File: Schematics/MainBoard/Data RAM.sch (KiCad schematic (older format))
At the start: 8 parts, among them U10 IDT71256SA12TPG, U11 IDT71256SA12TPG, U8 74LS32, U9 74LS04

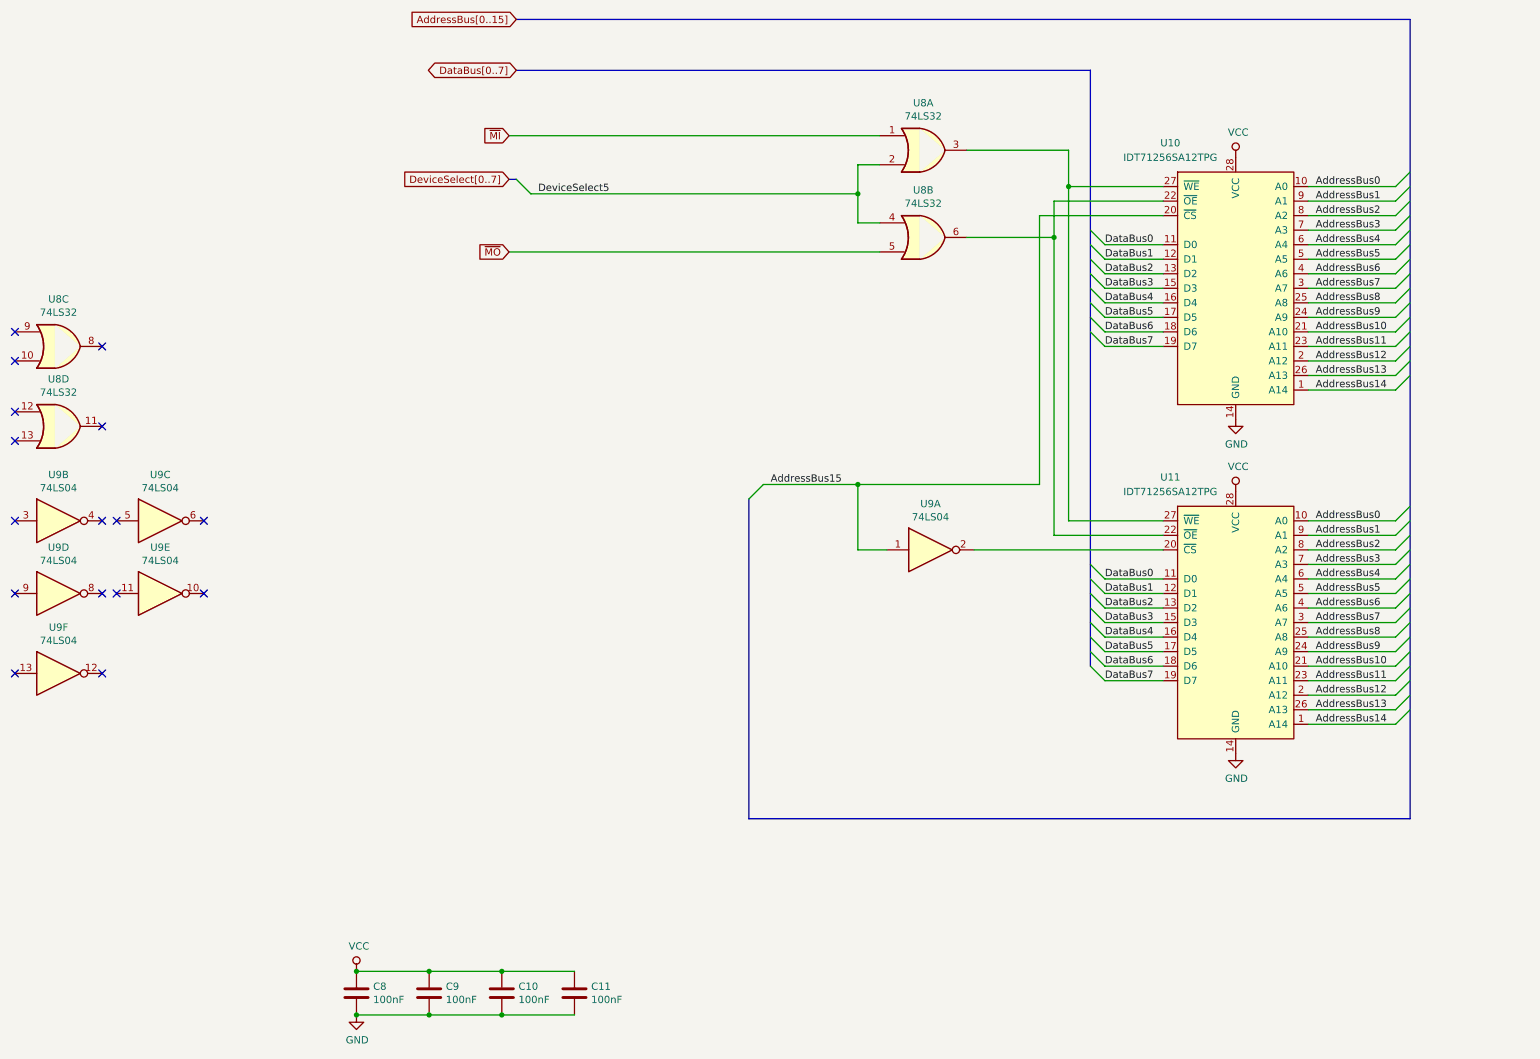
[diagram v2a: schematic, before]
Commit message: Added Data RAM submodule to main board again.
Staked out component positions on the PCB but did not route traces yet.
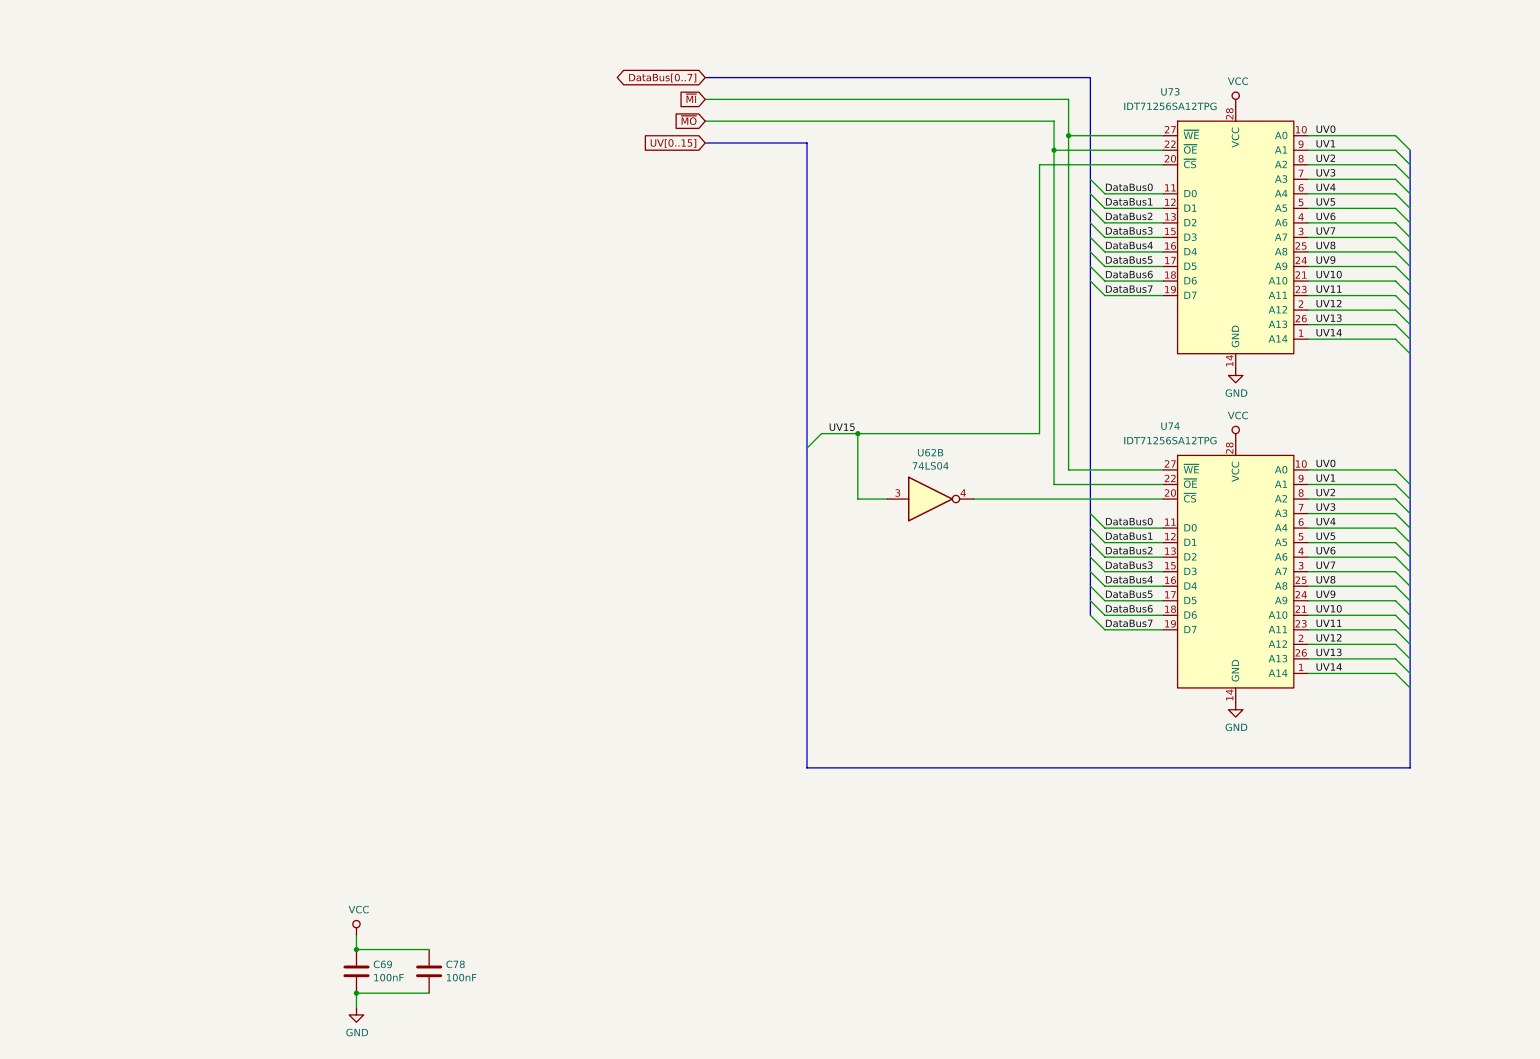
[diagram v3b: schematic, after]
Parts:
- removed C10, C11: 100nF, Capacitor_THT:C_Disc_D4.3mm_W1.9mm_P5.00mm, symbol Device:C
- removed U8: 74LS32, Package_DIP:DIP-14_W7.62mm, symbol 74xx:74LS32
- removed unit 2 of U9
- removed unit 4 of U9
- removed unit 3 of U9
- removed unit 5 of U9
- removed unit 6 of U9
- renumbered C8 to C69, C9 to C78, U9 to U62, U10 to U73, U11 to U74
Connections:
- net ~MI: now also U73.27 (~WE), U74.27 (~WE)
- net ~MO: now also U73.22 (~OE), U74.22 (~OE)
- net at U74.20 (~CS): now also U62.4; no longer U62.2
- net AddressBus0 renamed UV0
- net AddressBus1 renamed UV1
- net AddressBus10 renamed UV10
- net AddressBus11 renamed UV11
- net AddressBus12 renamed UV12
- net AddressBus13 renamed UV13
- net AddressBus14 renamed UV14
- net AddressBus15 renamed UV15
- net UV15: now also U62.3; no longer U62.1
- net AddressBus2 renamed UV2
- net AddressBus3 renamed UV3
- net AddressBus4 renamed UV4
- net AddressBus5 renamed UV5
- net AddressBus6 renamed UV6
- net AddressBus7 renamed UV7
- net AddressBus8 renamed UV8
- net AddressBus9 renamed UV9
- no-connect marks 16 -> 0
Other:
- moved on the sheet: C69, C78, U73, U74

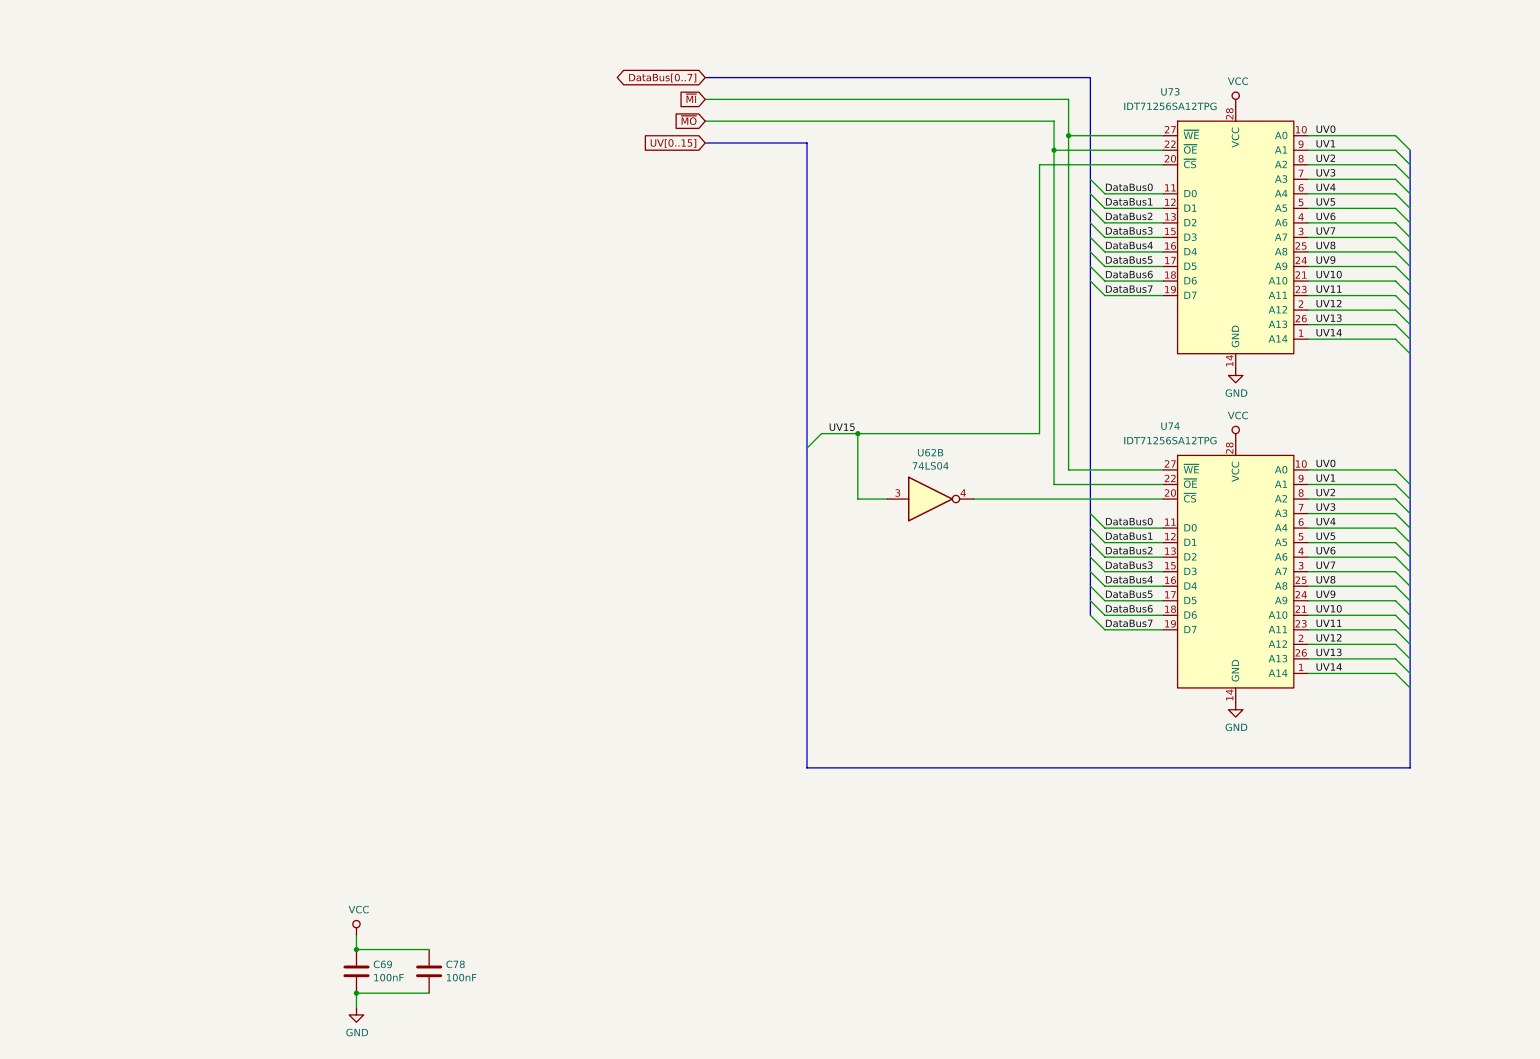
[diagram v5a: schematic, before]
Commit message: Begin work on the Rev 2 hardware.
* Four layer PCB for the main board
* Breaking the main board up into several smaller daughter boaeds.
* ZIF sockets for Instruction ROM
* Dual Port SRAM for Instruction RAM
* Daughter board connectors interleave signals and GND.
* DC Barrel jack connector for power
* WIP shifter circuit
* Rename SharedMemoryArduinoSerialCard to SerialCard.
* TurtleTTL Rev 2 will use the shared memory serial card.
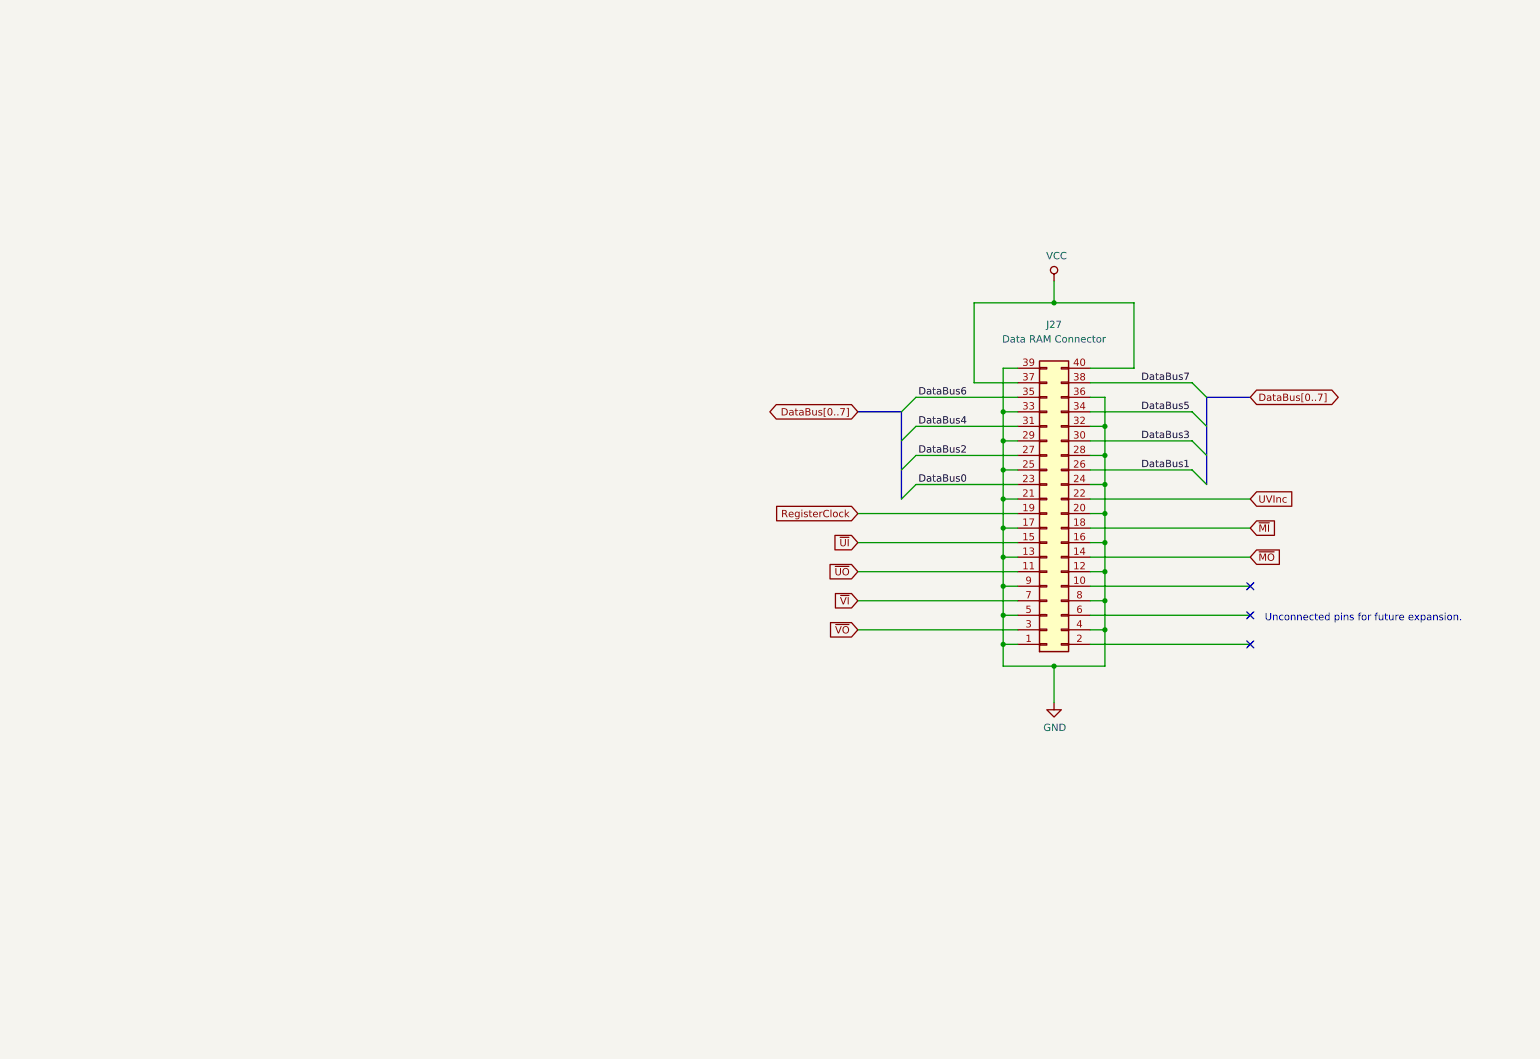
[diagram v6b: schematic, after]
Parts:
- removed C69, C78: 100nF, Capacitor_THT:C_Disc_D4.3mm_W1.9mm_P5.00mm, symbol Device:C
- removed U62: 74LS04, Package_DIP:DIP-14_W7.62mm, symbol 74xx:74LS04
- removed U73, U74: IDT71256SA12TPG, Package_DIP:DIP-28_W7.62mm_Socket, symbol Memory_RAM:IDT71256SA12TPG
- added J27: Data RAM Connector, Connector_PinSocket_2.54mm:PinSocket_2x20_P2.54mm_Vertical, symbol Connector_Generic:Conn_02x20_Odd_Even
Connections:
- net DataBus0: now also J27.23 (Pin_23)
- net DataBus1: now also J27.26 (Pin_26)
- net DataBus2: now also J27.27 (Pin_27)
- net DataBus3: now also J27.30 (Pin_30)
- net DataBus4: now also J27.31 (Pin_31)
- net DataBus5: now also J27.34 (Pin_34)
- net DataBus6: now also J27.35 (Pin_35)
- net DataBus7: now also J27.38 (Pin_38)
- net GND: now also J27.1 (Pin_1), J27.12 (Pin_12), J27.13 (Pin_13), J27.16 (Pin_16), J27.17 (Pin_17), J27.20 (Pin_20), J27.21 (Pin_21), J27.24 (Pin_24), J27.25 (Pin_25), J27.28 (Pin_28), J27.29 (Pin_29), J27.32 (Pin_32), J27.33 (Pin_33), J27.36 (Pin_36), J27.39 (Pin_39), J27.4 (Pin_4), J27.5 (Pin_5), J27.8 (Pin_8), J27.9 (Pin_9)
- net VCC: now also J27.37 (Pin_37), J27.40 (Pin_40)
- net ~MI: now also J27.18 (Pin_18)
- net ~MO: now also J27.14 (Pin_14)
- new net RegisterClock: J27.19 (Pin_19)
- new net UVInc: J27.22 (Pin_22)
- new net ~UI: J27.15 (Pin_15)
- new net ~UO: J27.11 (Pin_11)
- new net ~VI: J27.7 (Pin_7)
- new net ~VO: J27.3 (Pin_3)
- no-connect marks 0 -> 3
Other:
- note added: "Unconnected pins for future expansion."
